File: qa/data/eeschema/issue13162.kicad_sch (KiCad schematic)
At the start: 31 parts, among them M1 IRFP240, M2 IRFP240, U1 TL072

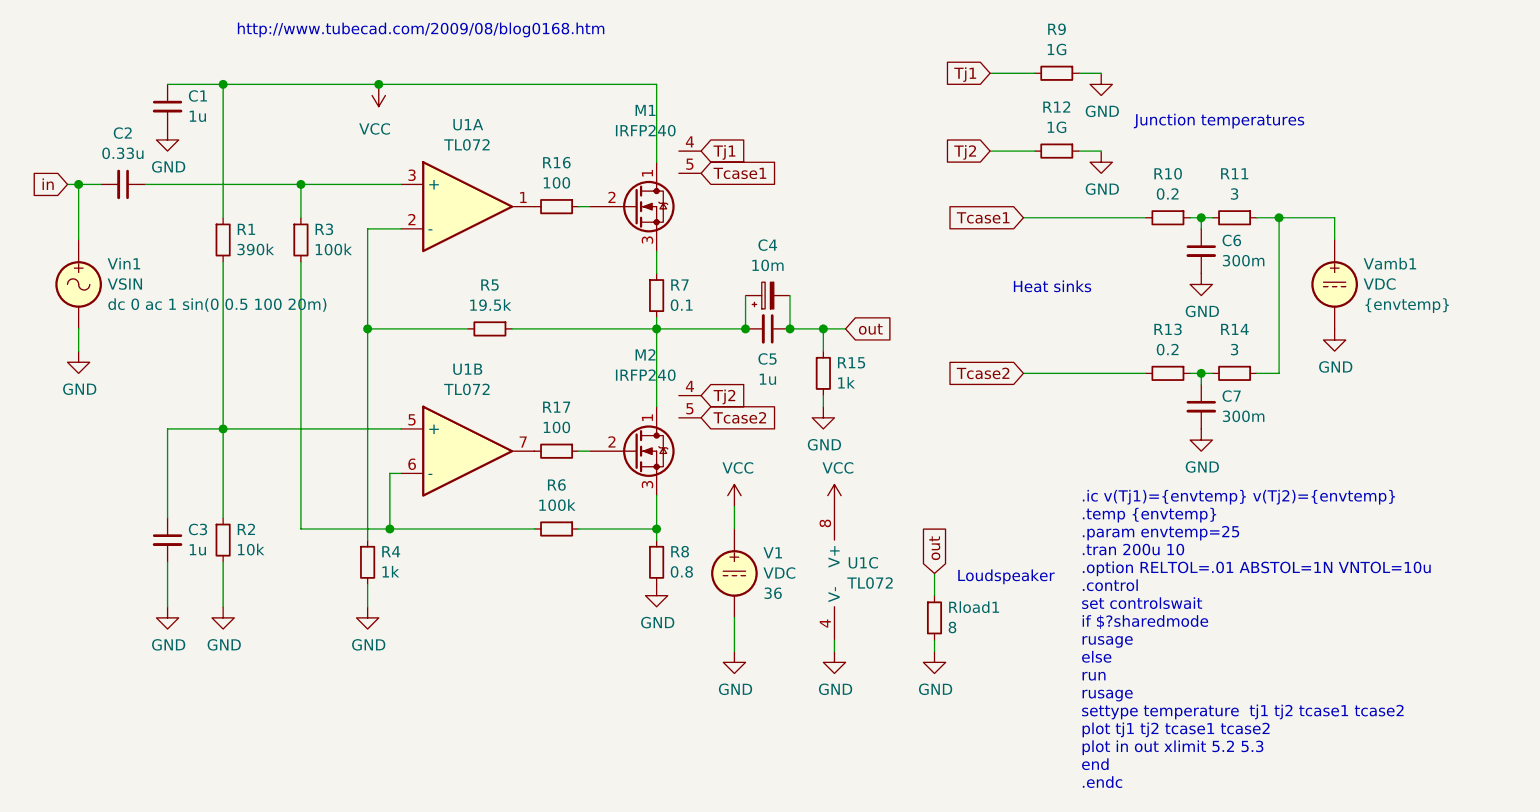
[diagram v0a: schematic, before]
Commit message: Change regression test for #13162 to be less complex
We are really only testing that `Rload1` works,
and the original testcase is unstable on some platforms.
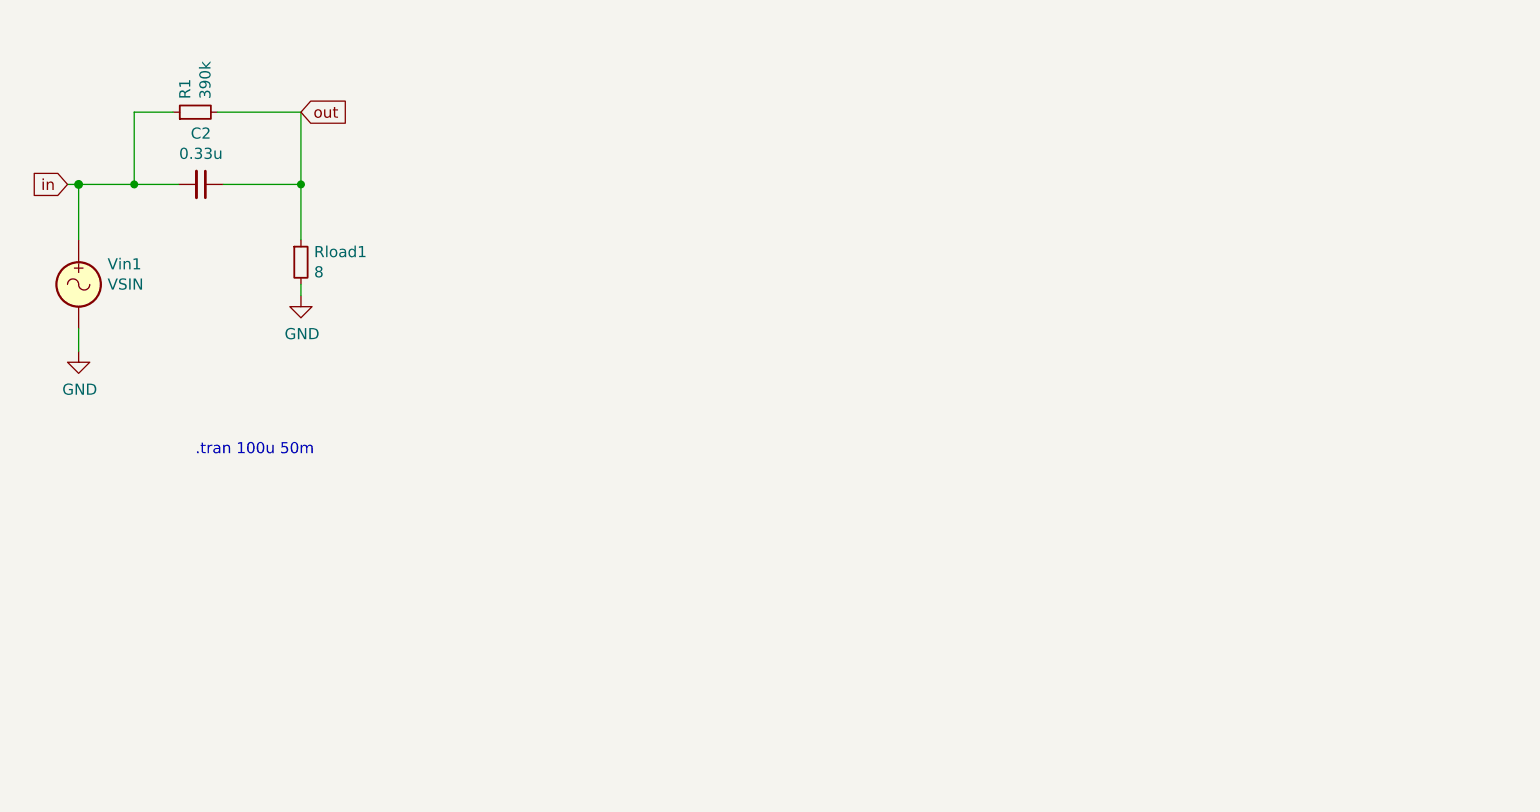
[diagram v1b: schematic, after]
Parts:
- removed C1, C3, C5: 1u, symbol Device:C_Small
- removed C4: 10m, symbol Device:CP_Small
- removed C6, C7: 300m, symbol Device:C_Small
- removed M1, M2: IRFP240, symbol HVO_Device:Q_NMOS_DGS_T
- removed R10, R13: 0.2, symbol Device:R_Small
- removed R11, R14: 3, symbol Device:R_Small
- removed R12, R9: 1G, symbol Device:R_Small
- removed R15, R4: 1k, symbol Device:R_Small
- removed R16, R17: 100, symbol Device:R_Small
- removed R2: 10k, symbol Device:R_Small
- removed R3, R6: 100k, symbol Device:R_Small
- removed R5: 19.5k, symbol Device:R_Small
- removed R7: 0.1, symbol Device:R_Small
- removed R8: 0.8, symbol Device:R_Small
- removed U1: TL072, symbol Device:Opamp_Dual_Generic
- removed V1, Vamb1: VDC, symbol Simulation_SPICE:VDC
- Vin1: Spice_Model dc 0 ac 1 sin(0 0.5 100 20m) -> (none); Spice_Netlist_Enabled Y -> (none); Spice_Primitive V -> (none)
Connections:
- net VCC is gone; now on net in: R1.1
- net out: now also C2.1, R1.2
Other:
- note added: ".tran 100u 50m"
- note removed: ".ic v(Tj1)={envtemp} v(Tj2)={envtemp} .temp {envtemp} .param envtemp=25 .tran 200u 10 .option RELTOL=.01 ABSTOL=1N VNTOL=10u .control set controlswait if $?sharedmode rusage else run rusage settype temperature tj1 tj2 tcase1 tcase2 plot tj1 tj2 tcase1 tcase2 plot in out xlimit 5.2 5.3 end .endc"
- note removed: "Heat sinks"
- note removed: "Junction temperatures"
- note removed: "Loudspeaker"
- note removed: "http://www.tubecad.com/2009/08/blog0168.htm"
- moved on the sheet: C2, R1, Rload1
